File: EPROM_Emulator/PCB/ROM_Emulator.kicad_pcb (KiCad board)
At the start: 2 copper layers, 21.5 x 37.1 mm, 5 parts, among them U1 27C512, U2 74LS245, U3 Teensy4.0, U4 74LS245, U5 74LS245

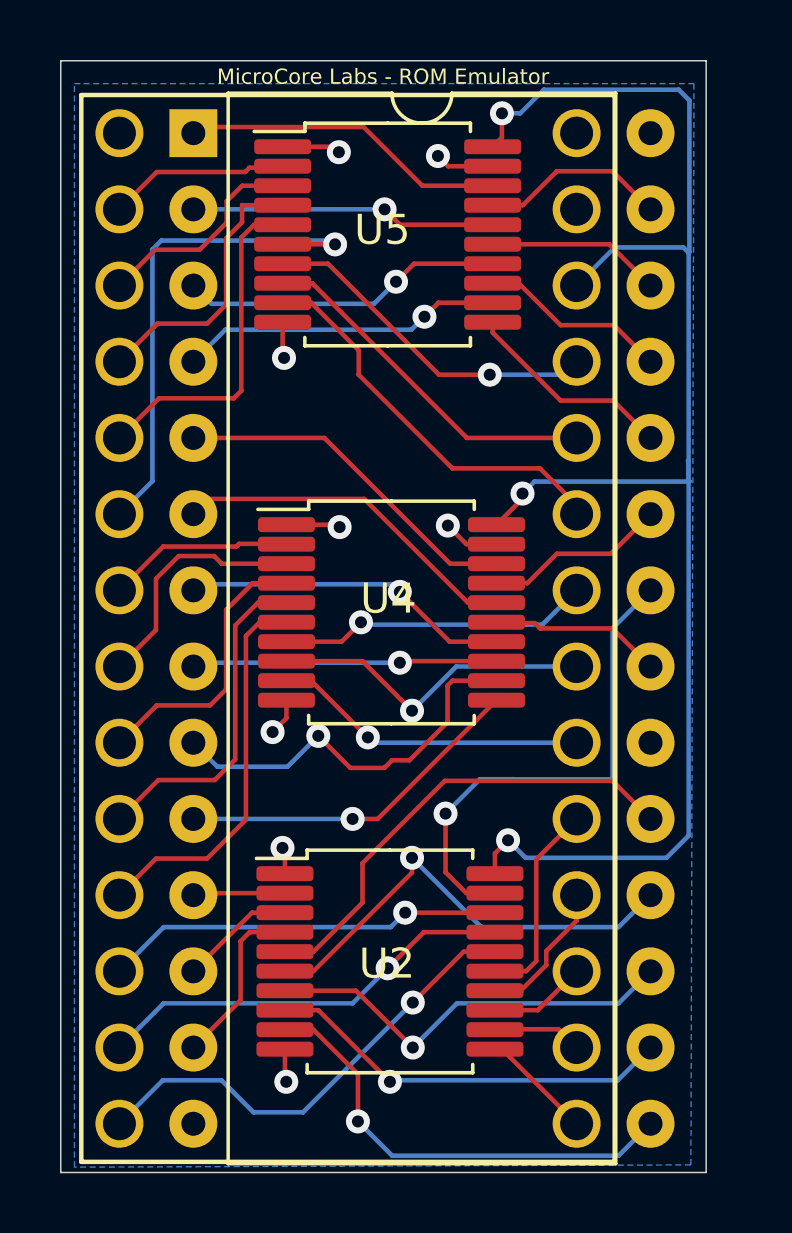
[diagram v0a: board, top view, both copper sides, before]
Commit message: Delete unnecessary auto generated files, Upgrade project to KiCAD 6.10, Moved custom symbols and footprints to Project specific files, Clean up PCB traces and overall layout, Add README with some instructions, Add PCB renders.
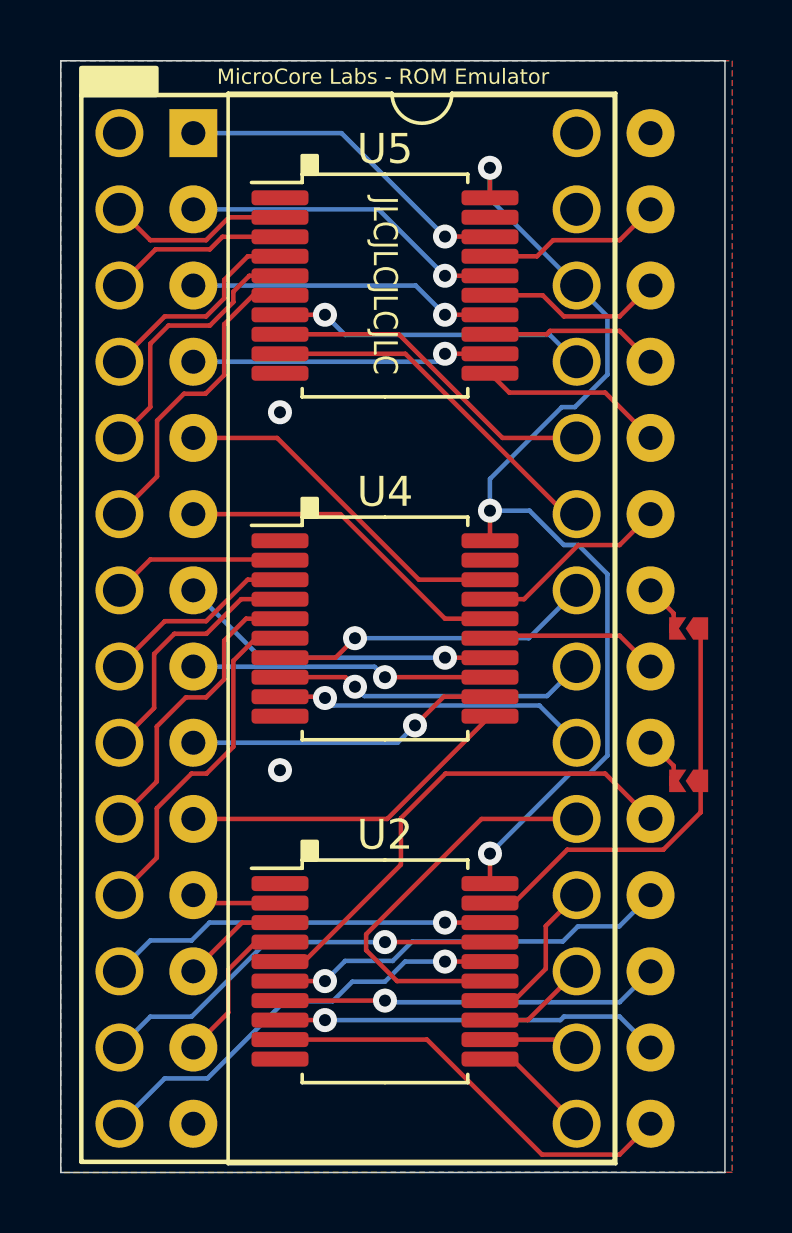
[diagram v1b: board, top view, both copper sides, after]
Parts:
- added REF_D9: SolderJumper-2_P1.3mm_Open_TrianglePad1.0x0.75mm, A_Personal_Library:SolderJumper-2_P1.3mm_Open_TrianglePad1.0x0.75mm, F.Cu at (183.5, 105.5)
- added REF_D9: SolderJumper-2_P1.3mm_Open_TrianglePad1.0x0.75mm, A_Personal_Library:SolderJumper-2_P1.3mm_Open_TrianglePad1.0x0.75mm, F.Cu at (183.5, 100.5)
- moved U5 1.70 mm to (173.4, 89.0)
- moved U4 0.58 mm to (173.4, 100.5)
- moved U2 0.37 mm to (173.4, 111.9)
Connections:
- U1 pad 20: Net-(U1-Pad20) -> CS_20
- U1 pad 22: OE_n -> CS_22
- U1 pad 28: Net-(U1-Pad28) -> unconnected-(U1-Pad28)
- U3 pad 33: Net-(U3-Pad33) -> unconnected-(U3-Pad33)
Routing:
- net +3V3: track 52.9 -> 34.0 mm
- net GND: track 12.1 -> 0.00 mm, vias 8 -> 2
- net V3_D7: track 6.81 -> 13.7 mm
- net V3_A7: track 17.3 -> 10.5 mm, vias 1 -> 0
- net V5_A1: track 14.0 -> 10.5 mm
- net V3_A12: track 9.97 -> 7.17 mm
- net OE_n: track 16.8 -> 14.4 mm, vias 1 -> 0
- net V3_A13: track 11.4 -> 9.03 mm
- net V5_D6: track 15.4 -> 13.5 mm
- net V3_A14: track 7.88 -> 6.02 mm
- net V3_A11: track 8.20 -> 6.55 mm
- net CS_20: track 0.00 -> 1.59 mm
- net CS_22: track 0.00 -> 1.59 mm
- net V3_A3: track 12.9 -> 11.5 mm
- net V5_D5: track 14.0 -> 12.8 mm
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- added copper zone on F.Cu, net GND
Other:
- board size 21.5 x 37.1 mm -> 22.1 x 37.1 mm
- net class Default removed
- board text added: "JLCJLCJLCJLC"
